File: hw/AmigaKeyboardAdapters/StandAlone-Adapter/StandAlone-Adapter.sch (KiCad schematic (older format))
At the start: 60 parts, among them J1 RJ10, J2 Conn_02x03_Odd_Even, P1 CONN_01X02, Q1 BSS138, Q2 BSS138, Q3 BSS138, U1 AZ1117-3.3, U3 STM32F401RCTx

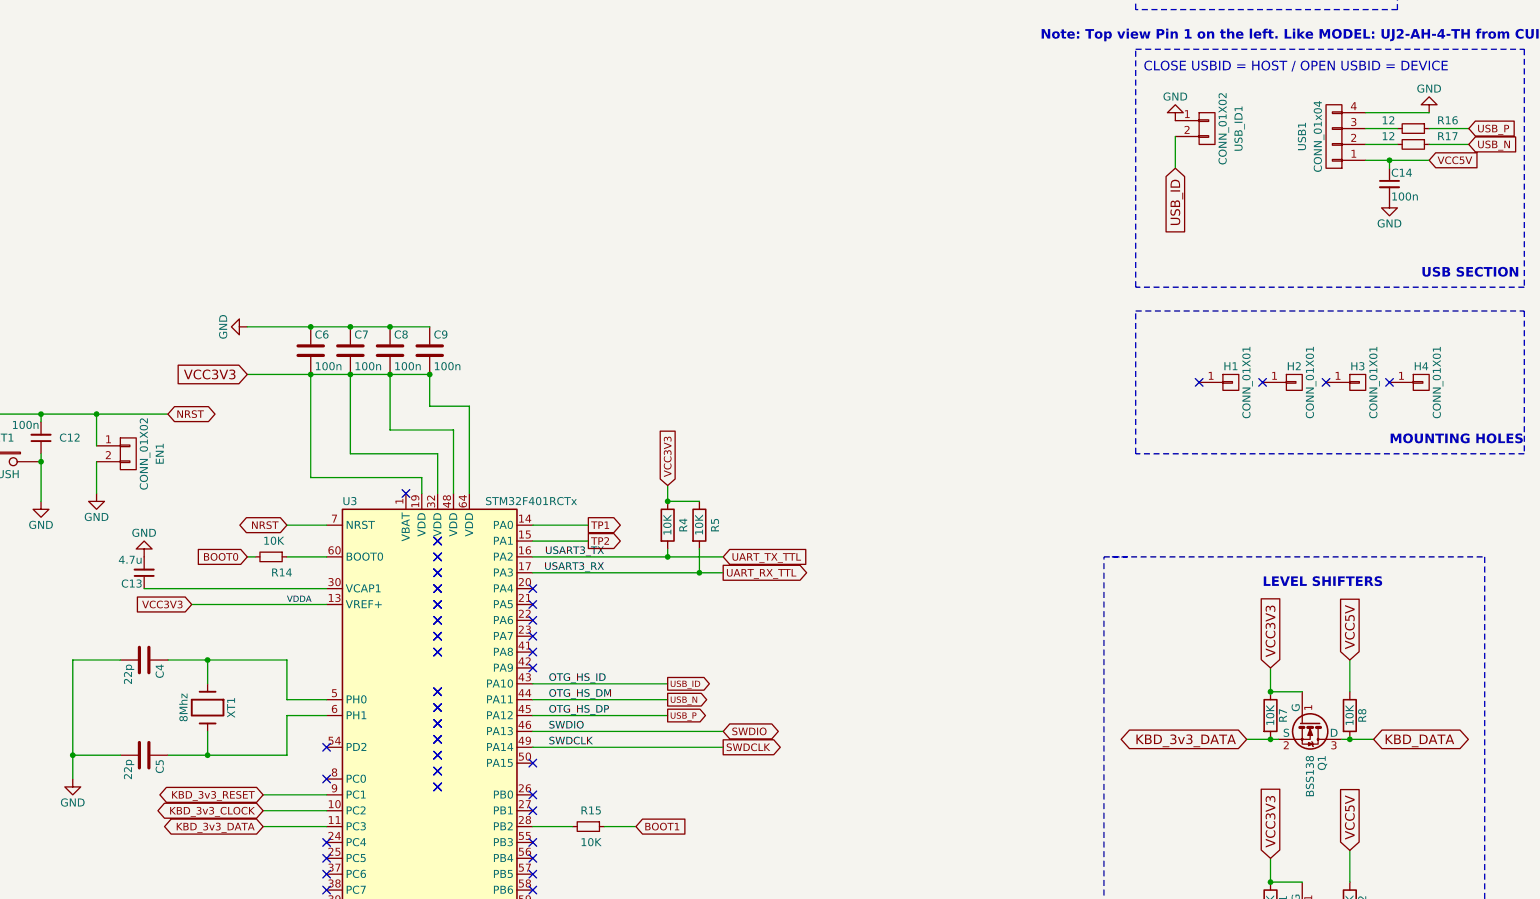
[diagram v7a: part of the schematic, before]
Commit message: Changed the capacitors for Crystal Oscillator. From 22pf to 20pf for 8Mhz
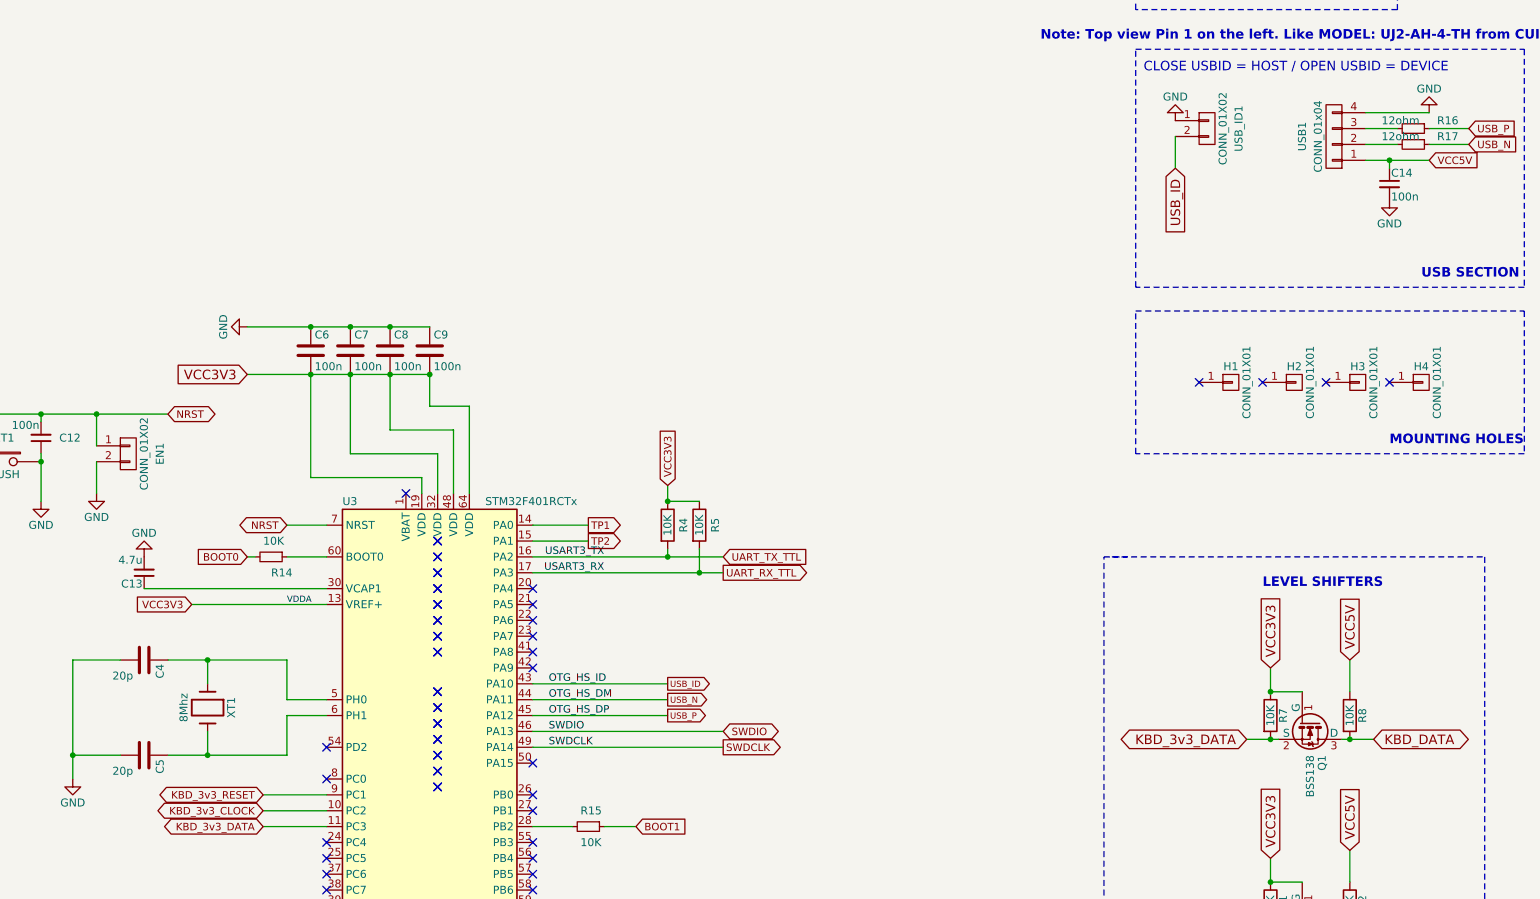
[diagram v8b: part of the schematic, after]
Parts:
- C4, C5: value 22p -> 20p
- R16, R17: value 12 -> 12ohm
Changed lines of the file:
@@
 P 6800 5450
 F 0 "C4" H 6825 5550 50  0000 L CNN
-F 1 "22p" H 6825 5350 50  0000 L CNN
+F 1 "20p" V 6900 5250 50  0000 L CNN
 F 2 "Capacitors_SMD:C_1206_HandSoldering" H 6838 5300 50  0001 C CNN
 F 3 "" H 6800 5450 50  0000 C CNN
@@
 P 6800 6050
 F 0 "C5" H 6825 6150 50  0000 L CNN
-F 1 "22p" H 6825 5950 50  0000 L CNN
+F 1 "20p" V 6900 5850 50  0000 L CNN
 F 2 "Capacitors_SMD:C_1206_HandSoldering" H 6838 5900 50  0001 C CNN
 F 3 "" H 6800 6050 50  0000 C CNN
@@
 P 14800 2100
 F 0 "R16" V 14750 2250 50  0000 L CNN
-F 1 "12" V 14750 1900 50  0000 L CNN
+F 1 "12ohm" V 14750 1900 50  0000 L CNN
 F 2 "Resistors_SMD:R_1206_HandSoldering" H 14800 2100 50  0001 C CNN
 F 3 "" H 14800 2100 50  0000 C CNN
@@
 P 14800 2200
 F 0 "R17" V 14750 2350 50  0000 L CNN
-F 1 "12" V 14750 2000 50  0000 L CNN
+F 1 "12ohm" V 14750 2000 50  0000 L CNN
 F 2 "Resistors_SMD:R_1206_HandSoldering" H 14800 2200 50  0001 C CNN
 F 3 "" H 14800 2200 50  0000 C CNN
